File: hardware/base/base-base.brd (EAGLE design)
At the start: 160 x 100 mm, 8 parts, among them U1 SD_CARD_SOCKET4UCON, X1 BU-SMA-V

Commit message: BASEHW: Added missing power bits, basically done now
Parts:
- added C1, C4: 22u, SparkFun-Capacitors:CAP-PTH-SMALL
- added C2, C5: 100n, SparkFun-Capacitors:CAP-PTH-SMALL
- added C3, C6: 47u, SparkFun-Capacitors:CAP-PTH-SMALL
- added L1: 2u2, resistor:0207/7
- added L2: 3u3, resistor:0207/7
- added R1: 33k2, resistor:VMTA55
- added R2, R4: 10k, resistor:VMTA55
- added R3: 56k2, resistor:VMTA55
- added U$4, U$5: TPS563200, FullyCustom:DDC0006A
- moved X1 155.2 mm to (54.6, 25.4), turned to 180 degrees
- moved U$2 149.3 mm to (29.2, 48.3), turned to 90 degrees
- moved U1 113.5 mm to (36.8, 64.8), turned to 90 degrees
- moved U$3 99.6 mm to (12.7, 101.6), turned to 270 degrees
- moved U$1 82.1 mm to (34.3, 64.8)
- moved Q1 29.3 mm to (-27.9, 128.3)
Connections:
- new net V+: C1.1, C4.1, U$4.3, U$4.5, U$5.3
- new net VREG_3_SW: C2.2, L1.1, U$4.2
- new net VREG_3_VBST: C2.1, U$4.6
- new net VREG_3_VFB: R1.1, R2.2, U$4.4
- new net VREG_5_SW: C5.2, L2.1, U$5.2
- new net VREG_5_VBST: C5.1, U$5.6
- new net VREG_5_VFB: R3.1, R4.2, U$5.4
- net +3V3: now also C3.1, L1.2, R1.2
- net +5V: now also C6.1, L2.2, R3.2
- net GND: now also C1.2, C3.2, C4.2, C6.2, R2.1, R4.1, U$4.1, U$5.1
- net GSM_PWR: now also U$1.P$82, U$5.5

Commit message: BASEHW: Radio routed
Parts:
- moved Q3 237.5 mm to (157.5, 132.1)
- moved Q2 207.0 mm to (138.4, 134.6)
- moved U$3 134.9 mm to (123.2, 179.1)
- moved Q1 83.9 mm to (55.9, 130.8)
- moved C2 71.2 mm to (-40.6, 12.7)
- moved X1 68.1 mm to (38.1, 91.4)
- moved R2 67.4 mm to (-54.6, 11.4)
- moved C3 66.5 mm to (-48.3, 14.0)
- moved U$4 66.3 mm to (-41.9, 16.5)
- moved C1 64.2 mm to (-49.5, 19.1)
- moved L1 63.8 mm to (-44.5, 8.89)
- moved R1 59.5 mm to (-52.1, 2.54)
- moved U1 55.8 mm to (53.3, 118.1)
- moved U$2 33.4 mm to (24.1, 81.3), turned to 270 degrees
- moved R4 20.5 mm to (-82.5, -48.3)
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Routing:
- net GND: track 0.00 -> 80.2 mm
- net RADIO_ANT: track 0.00 -> 34.2 mm
- net RADIO_MOSI: track 0.00 -> 31.6 mm
- net RADIO_CS: track 0.00 -> 30.2 mm
- net RADIO_MISO: track 0.00 -> 24.7 mm
- net RADIO_SCK: track 0.00 -> 24.3 mm
- net +3V3: track 0.00 -> 2.54 mm
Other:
- outline, holes or cut-outs redrawn

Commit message: BASEHW: Yayy, hardware design done
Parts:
- added C7: 100u, SparkFun-Passives:CPOL-RADIAL-10UF-25V
- added DEBUG: (no value), pinhead:1X06
- added PWR: (no value), pinhead:1X02
- L1, L2: device resistor:0207/7 -> resistor:0207/2V
- R1, R2, R3, R4: device resistor:VMTA55 -> resistor:0204/5
- moved C6 147.5 mm to (24.1, 17.1), turned to 180 degrees
- moved C4 146.5 mm to (21.0, 11.4), turned to 90 degrees
- moved C5 143.4 mm to (15.2, 15.9)
- moved U$3 142.2 mm to (16.5, 85.1)
- moved L2 135.8 mm to (24.1, 14.0), turned to 90 degrees
- moved Q3 132.3 mm to (52.1, 52.1)
- moved U$5 127.6 mm to (16.5, 12.7), flipped to the bottom
- moved R1 120.8 mm to (33.0, 88.3), turned to 270 degrees
- moved R3 115.1 mm to (8.89, 14.0), turned to 90 degrees
- moved R2 114.6 mm to (30.5, 88.3), turned to 90 degrees
- moved R4 112.7 mm to (11.4, 14.0), turned to 270 degrees
- moved Q2 104.6 mm to (50.8, 77.5)
- moved L1 101.4 mm to (17.8, 88.9), turned to 270 degrees
- moved C1 101.0 mm to (21.0, 91.4), turned to 270 degrees
- moved C2 100.3 mm to (26.7, 87.0), turned to 180 degrees
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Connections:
- net DEBUG_RX: now also DEBUG.4
- net DEBUG_TX: now also DEBUG.5
- net GND: now also C7.2, DEBUG.1, PWR.2
- net SD_PWR: now also U$1.P$75
- net V+: now also C7.1, PWR.1
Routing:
- net +5V: track 0.00 -> 192.1 mm, vias 0 -> 1
- net V+: track 0.00 -> 157.8 mm
- net GSM_PWR: track 0.00 -> 128.0 mm, vias 0 -> 3
- net +3V3: track 2.54 -> 126.4 mm, vias 0 -> 3
- net GND: track 80.2 -> 166.8 mm, vias 0 -> 2
- net N$2: track 0.00 -> 50.4 mm
- net RADIO_INT: track 0.00 -> 48.1 mm
- net DEBUG_TX: track 0.00 -> 40.7 mm, vias 0 -> 1
- net SD_DAT1: track 0.00 -> 39.5 mm
- net DEBUG_RX: track 0.00 -> 35.3 mm, vias 0 -> 1
- net SD_DAT0: track 0.00 -> 34.0 mm
- net RESET: track 0.00 -> 33.3 mm, vias 0 -> 1
- net N$1: track 0.00 -> 33.3 mm
- net GSM_TX: track 0.00 -> 32.1 mm, vias 0 -> 1
- net GSM_RX: track 0.00 -> 25.2 mm, vias 0 -> 1
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- added copper zone on layer 1, net GND
- added copper zone on layer 16, net GND
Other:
- board size 160 x 100 mm -> 76.2 x 101.3 mm

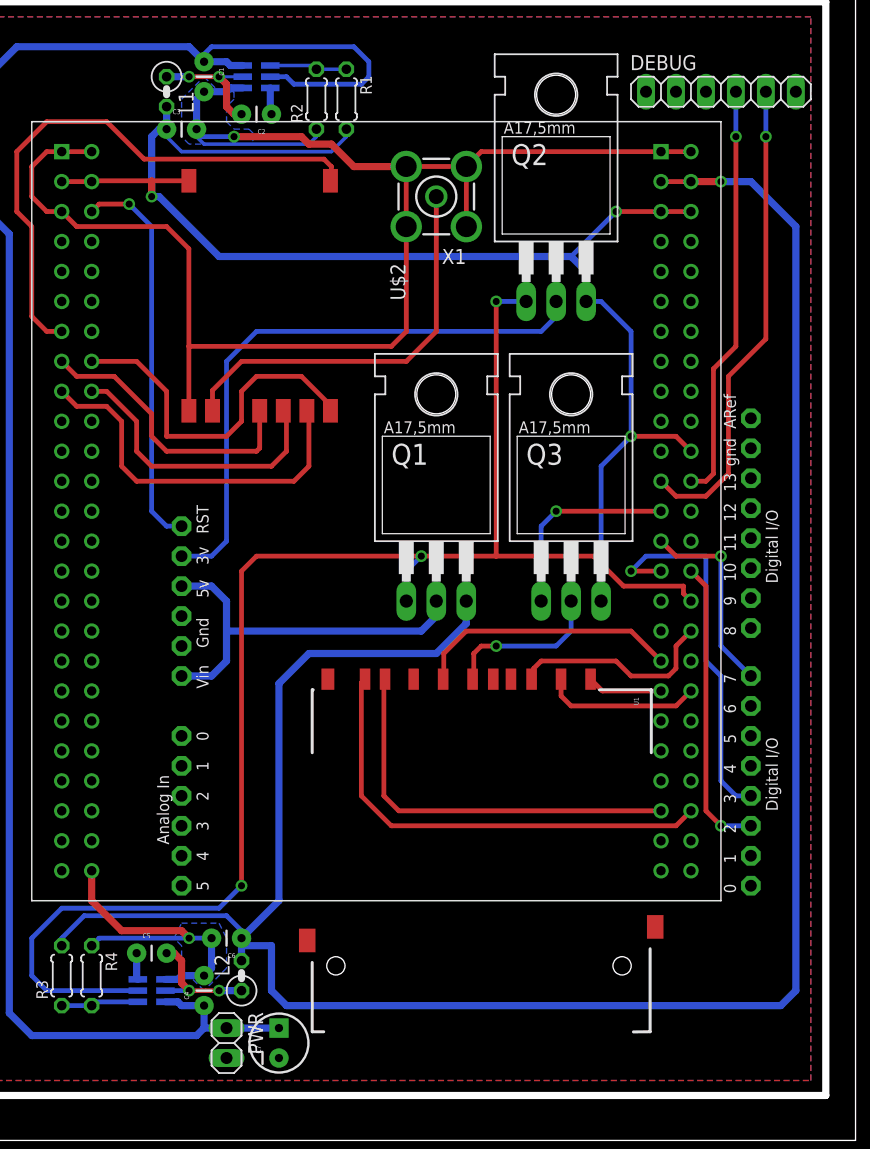
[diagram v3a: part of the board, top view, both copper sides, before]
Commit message: BASEHW: Pass for layout bugs, SD pullups
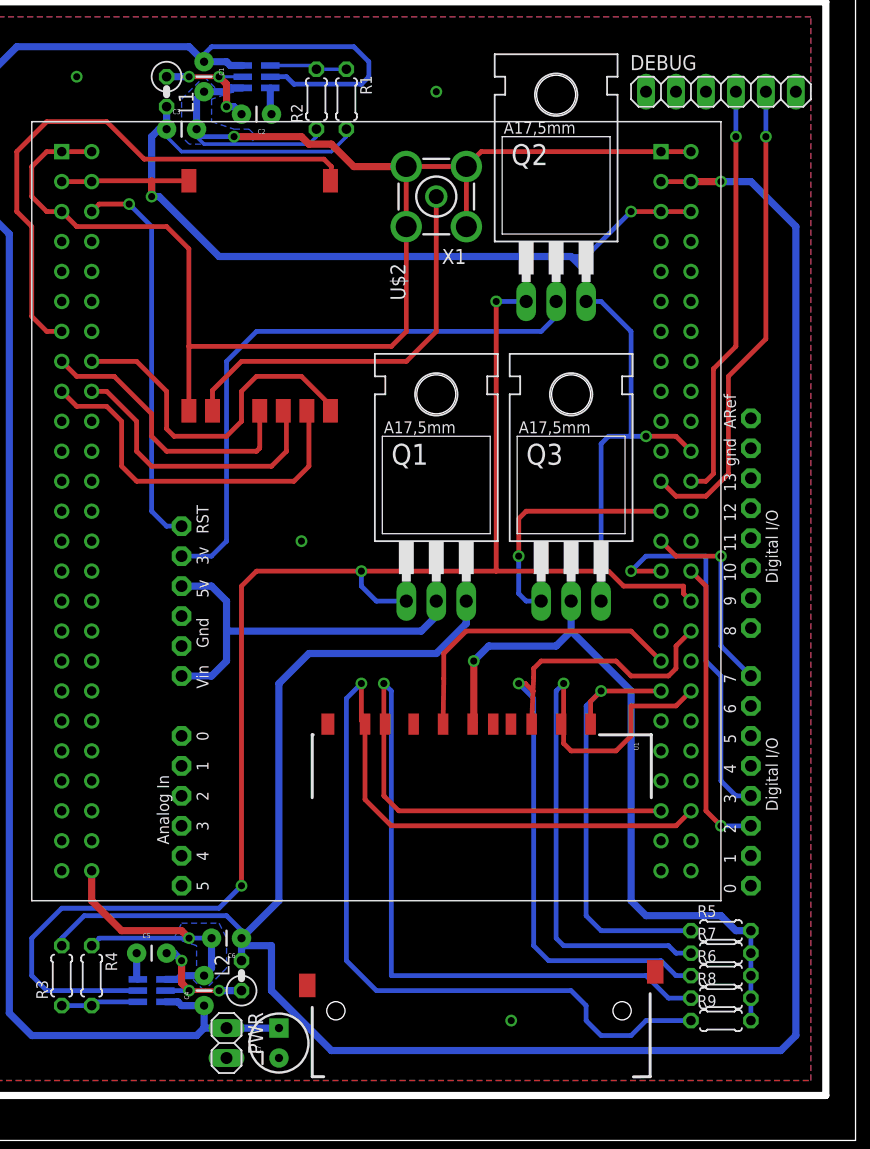
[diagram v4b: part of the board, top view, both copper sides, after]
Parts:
- added R5, R6, R7, R8, R9: 33k, resistor:0204/5
- moved U1 3.81 mm to (44.5, 34.3)
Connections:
- removed net N$3: Q3.D, U1.4
- new net SD_VCC: Q3.D, R5.2, R6.2, R7.2, R8.2, R9.2, U1.4
- net SD_CMD: now also R6.1
- net SD_DAT0: now also R8.1
- net SD_DAT1: now also R9.1
- net SD_DAT2: now also R5.1
- net SD_DAT3: now also R7.1
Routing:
- net SD_VCC: track 0.00 -> 61.0 mm, vias 0 -> 1
- net SD_DAT1: track 39.5 -> 96.2 mm, vias 0 -> 1
- net SD_DAT0: track 34.0 -> 84.9 mm, vias 0 -> 1
- net SD_CMD: track 17.8 -> 60.2 mm, vias 0 -> 1
- net SD_DAT3: track 13.3 -> 53.7 mm, vias 0 -> 1
- net SD_DAT2: track 6.38 -> 37.3 mm, vias 0 -> 1
- net N$3: track 13.8 -> 0.00 mm, vias 1 -> 0
- net +5V: track 192.1 -> 197.5 mm
- net SD_PWR: track 17.0 -> 20.8 mm
- net SD_CLK: track 22.5 -> 26.2 mm
- net +3V3: track 126.4 -> 127.5 mm
- net GSM_PWR: track 128.0 -> 128.8 mm
- net VREG_3_SW: vias 2 -> 3
- net VREG_5_SW: vias 2 -> 3
- net GND: vias 2 -> 6

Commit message: NODEHW: Layout cleanup. Also added base text
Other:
- board text added: "SBC-WSN sdn501 r:e59941"
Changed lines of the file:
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@@
 <wire x1="1.27" y1="96.52" x2="1.27" y2="3.81" width="0.6096" layer="20"/>
 <wire x1="1.27" y1="3.81" x2="73.66" y2="3.81" width="0.6096" layer="20"/>
+<text x="3.81" y="93.345" size="1.4224" layer="1" font="vector">SBC-WSN sdn501 r:e59941</text>
 </plain>
 <attributes>
@@
 </signal>
 </signals>
+<errors>
+</errors>
 </board>
 </drawing>

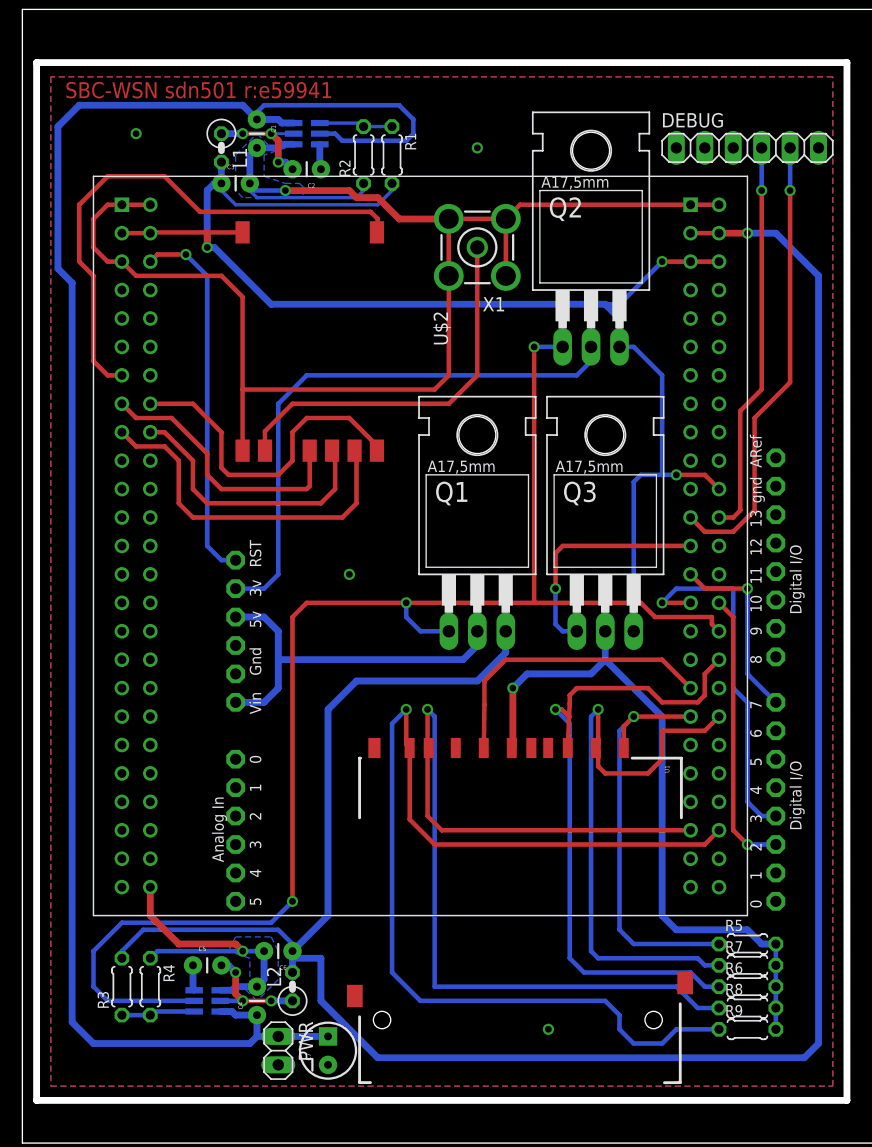
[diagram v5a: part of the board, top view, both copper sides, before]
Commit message: BASEHW: New inductors, larger resistors
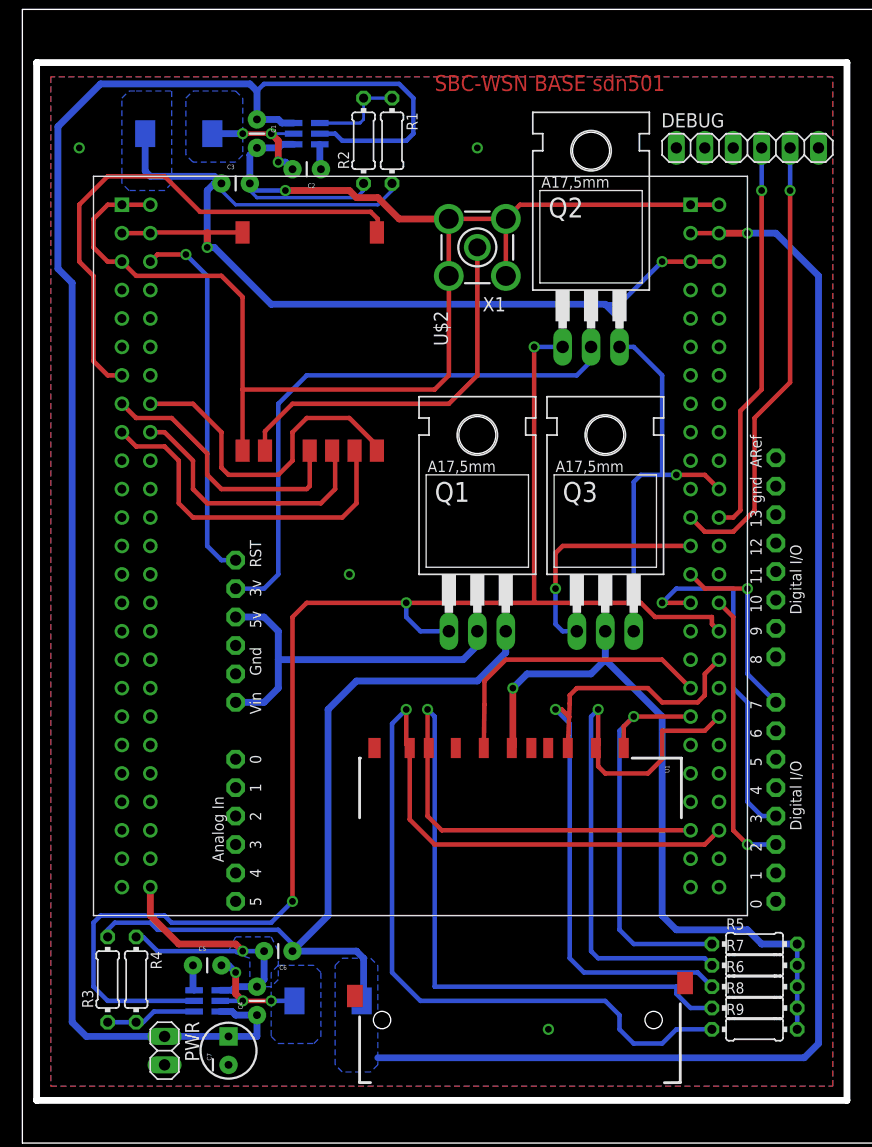
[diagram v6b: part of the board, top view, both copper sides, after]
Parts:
- L1, L2: device resistor:0207/2V -> FullyCustom:SRR7032
- R1, R2, R3, R4, R5, R6, R7, R8, R9: device resistor:0204/5 -> resistor:0204/7
- X1: value BU-SMA-V -> BU-SMA-1-7HOLE; device con-coax:BU-SMA-V -> FullyCustom:SMA_1-7HOLES
- moved PWR 10.2 mm to (12.7, 8.26)
- moved C7 8.89 mm to (18.4, 8.26)
- moved L1 4.02 mm to (14.0, 90.2), flipped to the bottom, turned to 90 degrees
- moved L2 3.42 mm to (27.3, 12.7), flipped to the bottom, turned to 270 degrees
- moved R3 1.42 mm to (7.62, 14.6)
- moved R4 1.42 mm to (10.2, 14.6)
- moved R1 1.27 mm to (33.0, 89.5)
- moved R2 1.27 mm to (30.5, 89.5)
- moved R5 0.64 mm to (65.4, 17.8)
- moved R6 0.64 mm to (65.4, 14.0)
- moved R7 0.64 mm to (65.4, 15.9)
- moved R8 0.64 mm to (65.4, 12.1)
- moved R9 0.64 mm to (65.4, 10.2)
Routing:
- net +3V3: track 127.5 -> 136.2 mm
- net +5V: track 197.5 -> 193.6 mm
- net V+: track 157.8 -> 155.3 mm
- net GSM_PWR: track 128.8 -> 130.8 mm
- net VREG_3_VFB: track 6.58 -> 8.49 mm
- net SD_VCC: track 61.0 -> 62.9 mm
- net VREG_5_VFB: track 6.58 -> 8.12 mm
- net GND: track 166.8 -> 168.3 mm
- net VREG_3_SW: track 10.8 -> 11.6 mm
- net SD_DAT2: track 37.3 -> 36.6 mm
- net SD_DAT3: track 53.7 -> 53.1 mm
- net SD_DAT1: track 96.2 -> 95.5 mm
- net SD_CMD: track 60.2 -> 59.5 mm
- added copper zone on layer 16, net +3V3
- added copper zone on layer 16, net +5V
- added copper zone on layer 16, net VREG_3_SW
- added copper zone on layer 16, net VREG_5_SW
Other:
- board text added: "SBC-WSN BASE sdn501"
- board text removed: "SBC-WSN sdn501 r:e59941"
